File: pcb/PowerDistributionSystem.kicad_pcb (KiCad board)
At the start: 4 copper layers, 66 x 60 mm, 51 parts, among them J2 PREC040DBAN-M71RC, U4 TMC2209-LA-T, U5 TMC2209-LA-T, U6 TMC2209-LA-T

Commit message: Assigned some nets to the connectors.
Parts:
- added JP1: SolderJumper_2_Open, Jumper:SolderJumper-2_P1.3mm_Open_RoundedPad1.0x1.5mm, F.Cu at (86.7, 99.7)
- added JP8: Jumper_2_Bridged, Jumper:SolderJumper-2_P1.3mm_Open_RoundedPad1.0x1.5mm, F.Cu at (86.7, 96.2)
- added R1: 1k, Resistor_SMD:R_1206_3216Metric_Pad1.30x1.75mm_HandSolder, F.Cu at (81.6, 99.9)
- added R3: 20k, Resistor_SMD:R_1206_3216Metric_Pad1.30x1.75mm_HandSolder, F.Cu at (81.6, 96.6)
- added TP1: TestPoint, TestPoint:TestPoint_Pad_1.0x1.0mm, F.Cu at (77.1, 100.0)
- added TP2: TestPoint, TestPoint:TestPoint_Pad_1.0x1.0mm, F.Cu at (77.1, 96.9)
- added U1: TPS22810DRV, Package_SON:WSON-6-1EP_2x2mm_P0.65mm_EP1x1.6mm, F.Cu at (73.7, 99.7)
- added U2: D24V7F5, pcb:D24V7Fx, F.Cu at (133.6, 117.2)
- added U3: D24V7F3, pcb:D24V7Fx, F.Cu at (142.9, 117.2)
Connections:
- net +BATT renamed +TE-RB
- net +EXTERNAL_A renamed +GSE-1
- net +EXTERNAL_B renamed +GSE-2
- net +EXTERNAL_C renamed +TE-RA
- J1 pad 1: unconnected-(J1-+3.3V-Pad1) -> +3.3V
- J1 pad 10: unconnected-(J1-GND-Pad10) -> GND
- J1 pad 11: unconnected-(J1-+3.3V-Pad11) -> +3.3V
- J1 pad 12: unconnected-(J1-uart_tx_A-Pad12) -> MOTOR_UART_TX
- J1 pad 13: unconnected-(J1-uart_rx_A-Pad13) -> MOTOR_UART_RX
- J1 pad 14: unconnected-(J1-GND-Pad14) -> GND
- J1 pad 17: unconnected-(J1-+3.3V-Pad17) -> +3.3V
- J1 pad 20: unconnected-(J1-GND-Pad20) -> GND
- J1 pad 21: unconnected-(J1-+3.3V-Pad21) -> +3.3V
- J1 pad 23: unconnected-(J1-GND-Pad23) -> GND
- J1 pad 25: unconnected-(J1-GND-Pad25) -> GND
- J1 pad 27: unconnected-(J1-+3.3V-Pad27) -> +3.3V
- J1 pad 3: unconnected-(J1-GND-Pad3) -> GND
- J1 pad 30: unconnected-(J1-GND-Pad30) -> GND
- J1 pad 31: unconnected-(J1-+3.3V-Pad31) -> +3.3V
- J1 pad 34: unconnected-(J1-GND-Pad34) -> GND
- J1 pad 37: unconnected-(J1-+3.3V-Pad37) -> +3.3V
- J1 pad 40: unconnected-(J1-GND-Pad40) -> GND
- J1 pad 41: unconnected-(J1-NC-Pad41) -> MOTOR_STEP_X
- J1 pad 42: unconnected-(J1-NC-Pad42) -> MOTOR_DIR_X
- J1 pad 43: unconnected-(J1-NC-Pad43) -> MOTOR_STEP_Y
- J1 pad 44: unconnected-(J1-NC-Pad44) -> MOTOR_DIR_Y
- J1 pad 45: unconnected-(J1-NC-Pad45) -> MOTOR_STEP_Z
- J1 pad 46: unconnected-(J1-NC-Pad46) -> MOTOR_DIR_Z
- J1 pad 47: unconnected-(J1-NC-Pad47) -> MOTOR_DISABLE
- J1 pad 5: unconnected-(J1-GND-Pad5) -> GND
- J1 pad 7: unconnected-(J1-+3.3V-Pad7) -> +3.3V
- J2 pad 21: BURNWIRE_VOLTAGE -> +TE-1
- J2 pad 22: unconnected-(J2-Pin_22-Pad22) -> +BATT-1
- J2 pad 24: unconnected-(J2-Pin_24-Pad24) -> GND
- J2 pad 25: BURNWIRE_VOLTAGE -> +TE-2
- J2 pad 26: unconnected-(J2-Pin_26-Pad26) -> +BATT-2
- J2 pad 28: unconnected-(J2-Pin_28-Pad28) -> GND
- J2 pad 29: unconnected-(J2-Pin_29-Pad29) -> +TE-3
- J2 pad 30: unconnected-(J2-Pin_30-Pad30) -> BURNWIRE_VOLTAGE
- J2 pad 31: unconnected-(J2-Pin_31-Pad31) -> GND
- J2 pad 32: unconnected-(J2-Pin_32-Pad32) -> GND

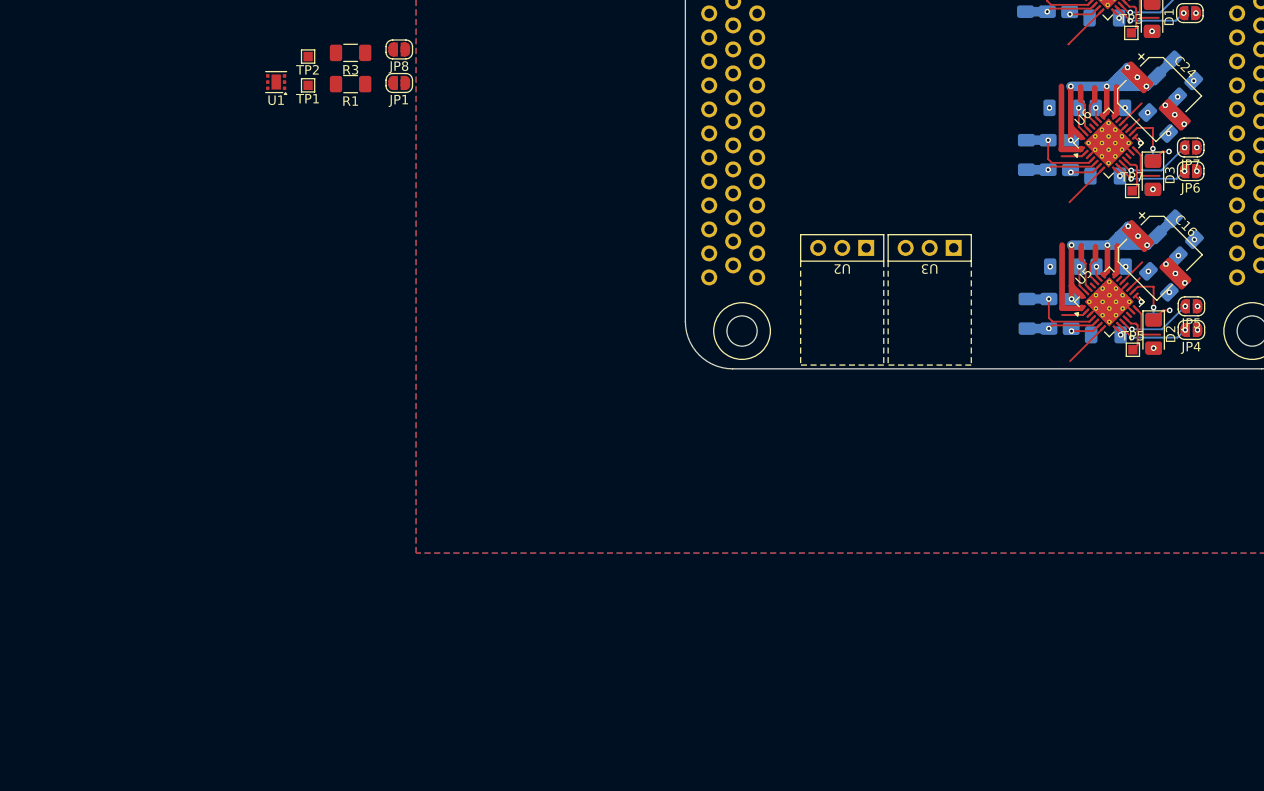
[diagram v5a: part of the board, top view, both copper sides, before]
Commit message: Added regulators for burn-wire.
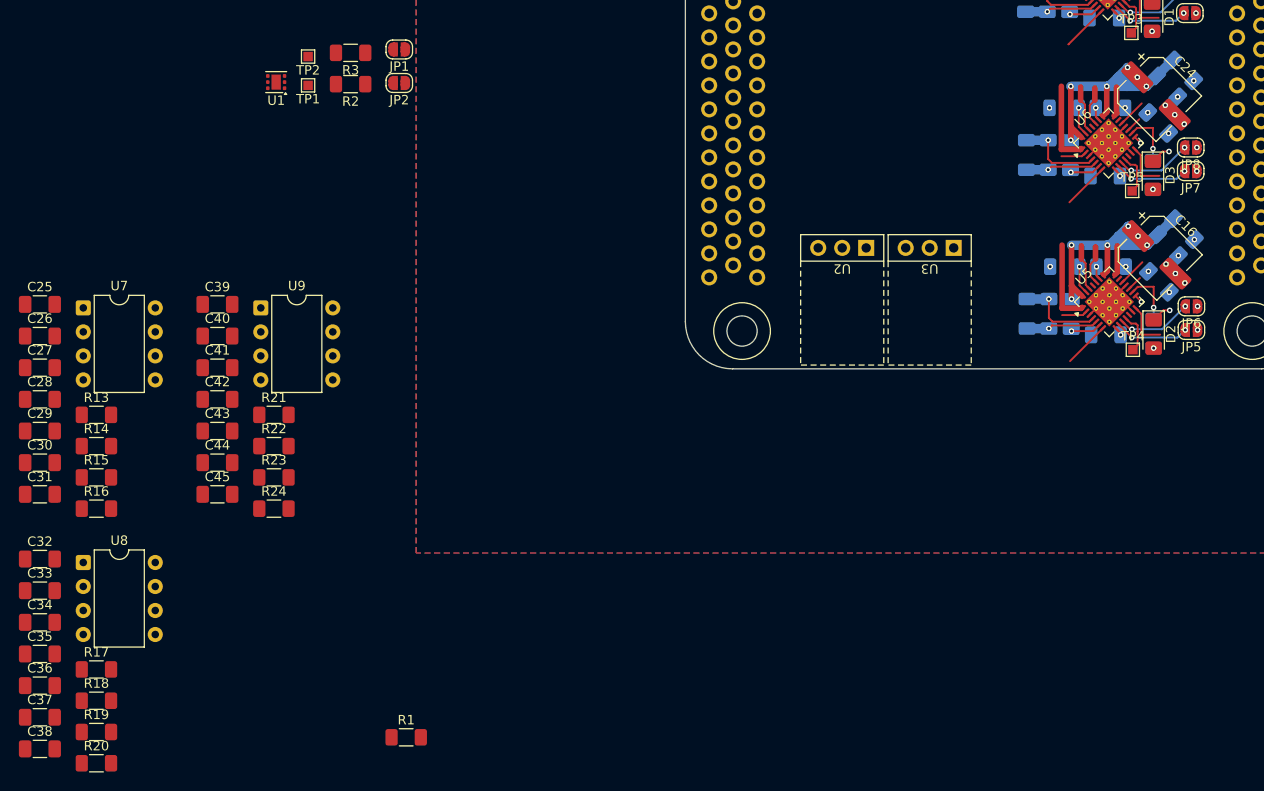
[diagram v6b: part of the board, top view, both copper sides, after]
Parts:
- added C25: 1n, Capacitor_SMD:C_1206_3216Metric_Pad1.33x1.80mm_HandSolder, F.Cu at (48.7, 123.2)
- added C26: 1n, Capacitor_SMD:C_1206_3216Metric_Pad1.33x1.80mm_HandSolder, F.Cu at (48.7, 126.5)
- added C27: 1n, Capacitor_SMD:C_1206_3216Metric_Pad1.33x1.80mm_HandSolder, F.Cu at (48.7, 129.9)
- added C28: 100n, Capacitor_SMD:C_1206_3216Metric_Pad1.33x1.80mm_HandSolder, F.Cu at (48.7, 133.2)
- added C29: 10n, Capacitor_SMD:C_1206_3216Metric_Pad1.33x1.80mm_HandSolder, F.Cu at (48.7, 136.6)
- added C30: 10n, Capacitor_SMD:C_1206_3216Metric_Pad1.33x1.80mm_HandSolder, F.Cu at (48.7, 139.9)
- added C31: 100n, Capacitor_SMD:C_1206_3216Metric_Pad1.33x1.80mm_HandSolder, F.Cu at (48.7, 143.3)
- added C32: 1n, Capacitor_SMD:C_1206_3216Metric_Pad1.33x1.80mm_HandSolder, F.Cu at (48.7, 150.1)
- added C33: 1n, Capacitor_SMD:C_1206_3216Metric_Pad1.33x1.80mm_HandSolder, F.Cu at (48.7, 153.5)
- added C34: 1n, Capacitor_SMD:C_1206_3216Metric_Pad1.33x1.80mm_HandSolder, F.Cu at (48.7, 156.8)
- added C35: 100n, Capacitor_SMD:C_1206_3216Metric_Pad1.33x1.80mm_HandSolder, F.Cu at (48.7, 160.2)
- added C36: 10n, Capacitor_SMD:C_1206_3216Metric_Pad1.33x1.80mm_HandSolder, F.Cu at (48.7, 163.5)
- added C37: 10n, Capacitor_SMD:C_1206_3216Metric_Pad1.33x1.80mm_HandSolder, F.Cu at (48.7, 166.9)
- added C38: 100n, Capacitor_SMD:C_1206_3216Metric_Pad1.33x1.80mm_HandSolder, F.Cu at (48.7, 170.2)
- added C39: 1n, Capacitor_SMD:C_1206_3216Metric_Pad1.33x1.80mm_HandSolder, F.Cu at (67.5, 123.2)
- added C40: 1n, Capacitor_SMD:C_1206_3216Metric_Pad1.33x1.80mm_HandSolder, F.Cu at (67.5, 126.5)
- added C41: 1n, Capacitor_SMD:C_1206_3216Metric_Pad1.33x1.80mm_HandSolder, F.Cu at (67.5, 129.9)
- added C42: 100n, Capacitor_SMD:C_1206_3216Metric_Pad1.33x1.80mm_HandSolder, F.Cu at (67.5, 133.2)
- added C43: 10n, Capacitor_SMD:C_1206_3216Metric_Pad1.33x1.80mm_HandSolder, F.Cu at (67.5, 136.6)
- added C44: 10n, Capacitor_SMD:C_1206_3216Metric_Pad1.33x1.80mm_HandSolder, F.Cu at (67.5, 139.9)
- added C45: 100n, Capacitor_SMD:C_1206_3216Metric_Pad1.33x1.80mm_HandSolder, F.Cu at (67.5, 143.3)
- added R1: 1k, Resistor_SMD:R_1206_3216Metric_Pad1.30x1.75mm_HandSolder, F.Cu at (87.5, 169.0)
- added R13: 20k, Resistor_SMD:R_1206_3216Metric_Pad1.30x1.75mm_HandSolder, F.Cu at (54.7, 134.9)
- added R14: 9k1, Resistor_SMD:R_1206_3216Metric_Pad1.30x1.75mm_HandSolder, F.Cu at (54.7, 138.2)
- added R15: 0, Resistor_SMD:R_1206_3216Metric_Pad1.30x1.75mm_HandSolder, F.Cu at (54.7, 141.5)
- added R16: 0, Resistor_SMD:R_1206_3216Metric_Pad1.30x1.75mm_HandSolder, F.Cu at (54.7, 144.8)
- added R17: 20k, Resistor_SMD:R_1206_3216Metric_Pad1.30x1.75mm_HandSolder, F.Cu at (54.7, 161.8)
- added R18: 9k1, Resistor_SMD:R_1206_3216Metric_Pad1.30x1.75mm_HandSolder, F.Cu at (54.7, 165.1)
- added R19: 0, Resistor_SMD:R_1206_3216Metric_Pad1.30x1.75mm_HandSolder, F.Cu at (54.7, 168.4)
- added R20: 0, Resistor_SMD:R_1206_3216Metric_Pad1.30x1.75mm_HandSolder, F.Cu at (54.7, 171.8)
- added R21: 20k, Resistor_SMD:R_1206_3216Metric_Pad1.30x1.75mm_HandSolder, F.Cu at (73.5, 134.9)
- added R22: 9k1, Resistor_SMD:R_1206_3216Metric_Pad1.30x1.75mm_HandSolder, F.Cu at (73.5, 138.2)
- added R23: 0, Resistor_SMD:R_1206_3216Metric_Pad1.30x1.75mm_HandSolder, F.Cu at (73.5, 141.5)
- added R24: 0, Resistor_SMD:R_1206_3216Metric_Pad1.30x1.75mm_HandSolder, F.Cu at (73.5, 144.8)
- added U7: L4978, Package_DIP:DIP-8_W7.62mm, F.Cu at (53.3, 123.5)
- added U8: L4978, Package_DIP:DIP-8_W7.62mm, F.Cu at (53.3, 150.5)
- added U9: L4978, Package_DIP:DIP-8_W7.62mm, F.Cu at (72.1, 123.5)
- U4, U5, U6: footprint pcb:VQFN-28-1EP_5x5mm_P0.5mm_EP3.7x3.7mm_ThermalVias -> Package_DFN_QFN:VQFN-28-1EP_5x5mm_P0.5mm_EP3.7x3.7mm_ThermalVias
- renumbered JP8 to JP1, JP1 to JP2, JP2 to JP3, JP3 to JP4, JP4 to JP5, JP5 to JP6, JP6 to JP7, JP7 to JP8, R1 to R2, TP5 to TP4, TP7 to TP5

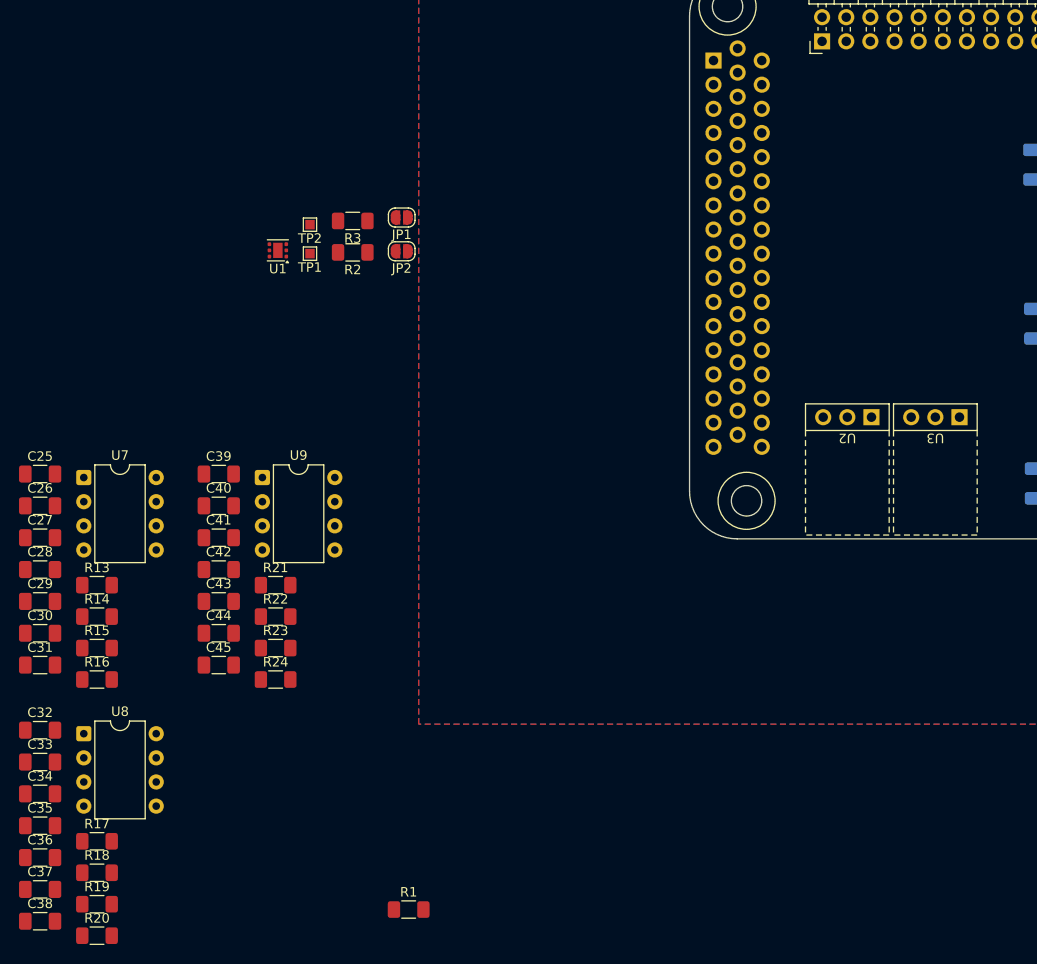
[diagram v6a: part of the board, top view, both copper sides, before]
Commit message: Routed L4978 burn-wire regulators.
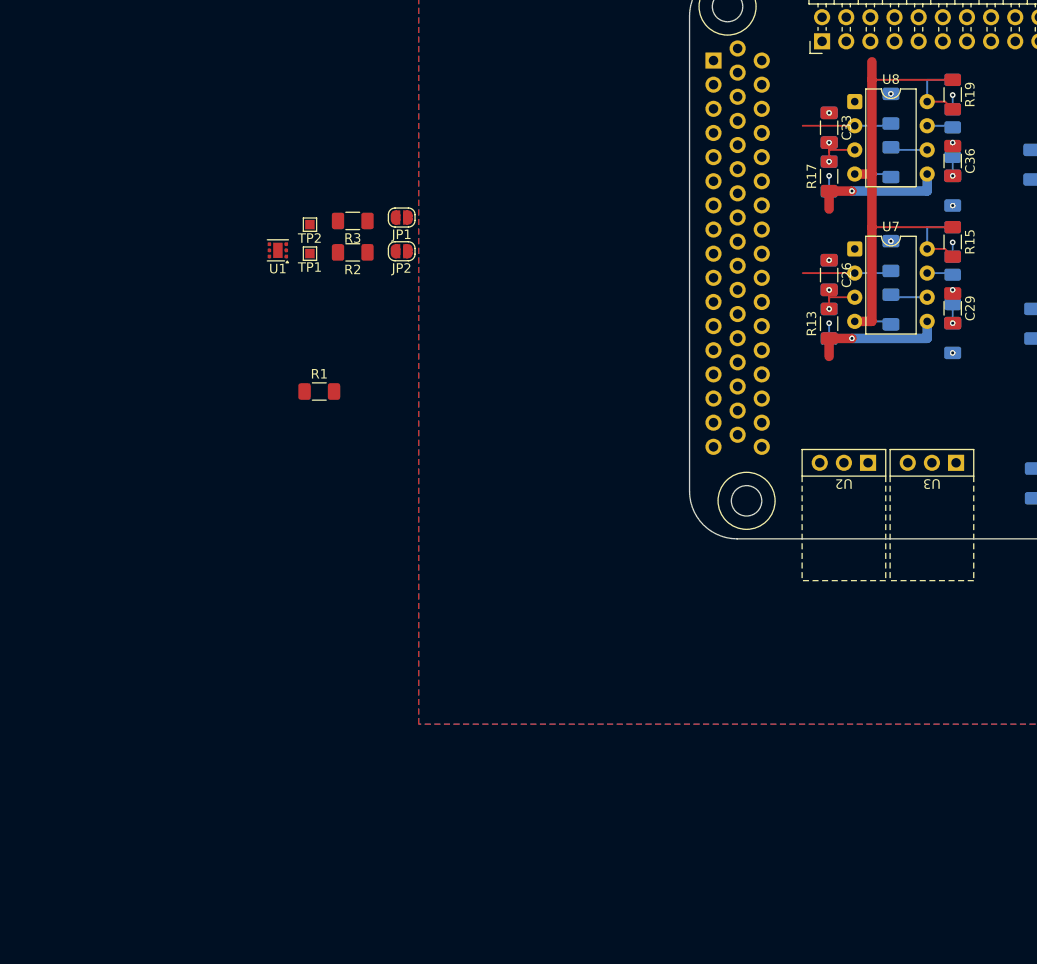
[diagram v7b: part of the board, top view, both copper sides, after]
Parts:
- removed C39, C40, C41: 1n, Capacitor_SMD:C_1206_3216Metric_Pad1.33x1.80mm_HandSolder
- removed C42, C45: 100n, Capacitor_SMD:C_1206_3216Metric_Pad1.33x1.80mm_HandSolder
- removed C43, C44: 10n, Capacitor_SMD:C_1206_3216Metric_Pad1.33x1.80mm_HandSolder
- removed R21: 20k, Resistor_SMD:R_1206_3216Metric_Pad1.30x1.75mm_HandSolder
- removed R22: 9k1, Resistor_SMD:R_1206_3216Metric_Pad1.30x1.75mm_HandSolder
- removed R23, R24: 0, Resistor_SMD:R_1206_3216Metric_Pad1.30x1.75mm_HandSolder
- removed U9: L4978, Package_DIP:DIP-8_W7.62mm
- C25, C27, C28, C30, C31, C32, C34, C35, C37, C38, R14, R16, R18, R20: moved to B.Cu
- moved R20 126.2 mm to (144.7, 83.3), turned to -90 degrees
- moved R19 123.9 mm to (144.7, 83.3), turned to -90 degrees
- moved C37 120.9 mm to (144.7, 93.4), turned to 90 degrees
- moved C36 120.8 mm to (144.7, 90.2), turned to -90 degrees
- moved C38 120.0 mm to (138.2, 90.4), turned to -90 degrees
- moved R18 118.4 mm to (144.7, 88.3), turned to -90 degrees
- moved C35 117.1 mm to (138.2, 84.7), turned to -90 degrees
- moved C34 108.6 mm to (131.7, 86.7), turned to -90 degrees
- moved C33 106.5 mm to (131.7, 86.7), turned to -90 degrees
- moved U8 104.9 mm to (134.4, 84.0)
- moved R17 104.1 mm to (131.7, 91.9), turned to 90 degrees
- moved C32 101.4 mm to (131.7, 91.9), turned to 90 degrees
- moved R16 101.1 mm to (144.7, 98.8), turned to -90 degrees
- moved C30 100.9 mm to (144.7, 108.9), turned to 90 degrees
- moved C29 100.8 mm to (144.7, 105.7), turned to -90 degrees
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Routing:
- net BURNWIRE_VOLTAGE: track 0.00 -> 55.8 mm
- net +BURNWIRE: track 0.00 -> 28.0 mm, vias 0 -> 2
- net BURNWIRE_ENABLE: track 0.00 -> 18.7 mm
- net Net-(U8-FB): track 0.00 -> 8.00 mm
- net Net-(U7-FB): track 0.00 -> 8.00 mm
- net GND: track 30.3 -> 37.3 mm, vias 27 -> 39
- net Net-(U8-OSC): track 0.00 -> 4.92 mm, vias 0 -> 2
- net Net-(U7-OSC): track 0.00 -> 4.92 mm, vias 0 -> 2
- net Net-(U8-BOOT): track 0.00 -> 3.93 mm
- net Net-(U7-BOOT): track 0.00 -> 3.93 mm
- net Net-(U8-COMP): track 0.00 -> 2.76 mm
- net Net-(U7-COMP): track 0.00 -> 2.76 mm
- net Net-(C36-Pad2): track 0.00 -> 2.00 mm, vias 0 -> 1
- net Net-(C29-Pad2): track 0.00 -> 2.00 mm, vias 0 -> 1
